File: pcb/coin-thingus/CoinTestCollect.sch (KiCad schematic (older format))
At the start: 10 parts, among them K3 AGQ200A4, K4 AGQ200A4, U3 H11AA1

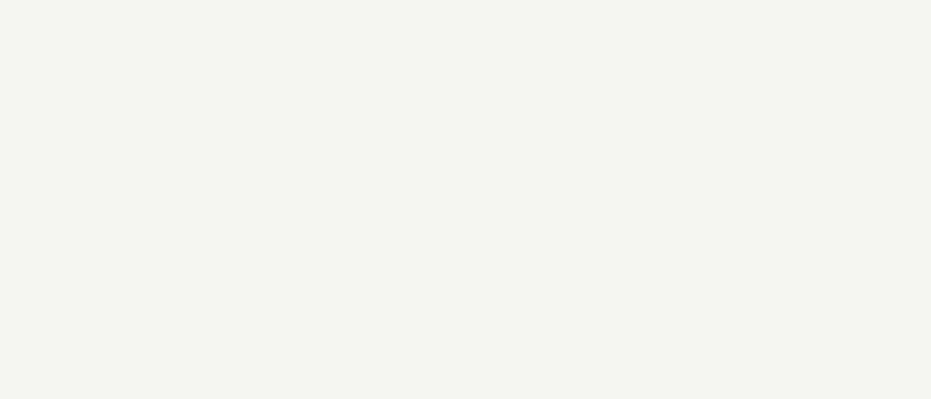
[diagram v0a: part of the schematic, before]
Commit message: Add CERN-OHL-W v2 license
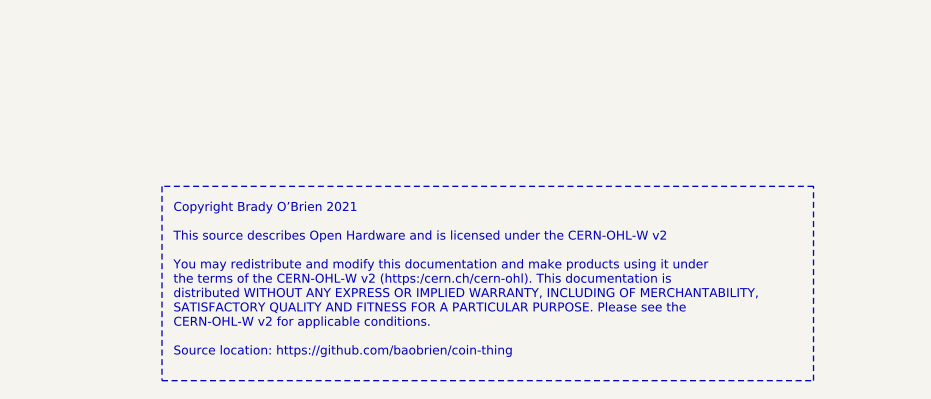
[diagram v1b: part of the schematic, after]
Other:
- note added: "Copyright Brady O’Brien 2021\n\nThis source describes Open Hardware and is licensed under the CERN-OHL-W v2\n\nYou may redistribute and modify this documentation and make products using it under\nthe terms of the CERN-OHL-W v2 (https:/cern.ch/cern-ohl). This documentation is\ndistributed WITHOUT ANY EXPRESS OR IMPLIED WARRANTY, INCLUDING OF MERCHANTABILITY,\nSATISFACTORY QUALITY AND FITNESS FOR A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"
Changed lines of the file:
@@
 Wire Wire Line
 	4050 2550 4200 2550
+Text Notes 8250 6300 0    39   ~ 0
+Copyright Brady O’Brien 2021\n\nThis source describes Open Hardware and is licensed under the CERN-OHL-W v2\n\nYou may redistribute and modify this documentation and make products using it under\nthe terms of the CERN-OHL-W v2 (https:/cern.ch/cern-ohl). This documentation is\ndistributed WITHOUT ANY EXPRESS OR IMPLIED WARRANTY, INCLUDING OF MERCHANTABILITY,\nSATISFACTORY QUALITY AND FITNESS FOR A PARTICULAR PURPOSE. Please see the\nCERN-OHL-W v2 for applicable conditions.\n\nSource location: https://github.com/baobrien/coin-thing
+Wire Notes Line
+	8200 5550 8200 6400
+Wire Notes Line
+	8200 6400 11050 6400
+Wire Notes Line
+	11050 6400 11050 5550
+Wire Notes Line
+	11050 5550 8200 5550
 $EndSCHEMATC

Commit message: Some work towards v0.2
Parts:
- removed U3: H11AA1, Package_DIP:DIP-6_W7.62mm, symbol Isolator:CNY17-1
- added U3: LTV-217, Package_SO:SOP-4_4.4x2.6mm_P1.27mm, symbol coin_trunker_parts:LTV-217
- K3: value AGQ200A4 -> HFD4/5-S
- R7: footprint Resistor_SMD:R_0612_1632Metric -> Resistor_SMD:R_1206_3216Metric
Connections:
- no-connect marks 1 -> 0
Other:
- moved on the sheet: R9
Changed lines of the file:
@@
 HV_P
-$Comp
-L Isolator:CNY17-1 U3
-U 1 1 5FA7F153
-P 8350 2900
-F 0 "U3" H 8500 3200 50  0000 C CNN
-F 1 "H11AA1" H 8350 3134 50  0000 C CNN
-F 2 "Package_DIP:DIP-6_W7.62mm" H 8350 2900 50  0001 L CNN
-F 3 "http://www.vishay.com/docs/83606/cny17.pdf" H 8350 2900 50  0001 L CNN
-	1    8350 2900
-	1    0    0    -1
-$EndComp
 $Comp
 L Device:R_US R8
@@
 F 0 "R7" H 7918 2546 50  0000 L CNN
 F 1 "3600R 2W" H 7918 2455 50  0000 L CNN
-F 2 "Resistor_SMD:R_0612_1632Metric" V 7890 2490 50  0001 C CNN
+F 2 "Resistor_SMD:R_1206_3216Metric" V 7890 2490 50  0001 C CNN
 F 3 "~" H 7850 2500 50  0001 C CNN
 	1    7850 2500
@@
 L Device:R_US R9
 U 1 1 5FAAD453
-P 8950 2700
-F 0 "R9" H 9018 2746 50  0000 L CNN
-F 1 "10K" H 9018 2655 50  0000 L CNN
-F 2 "Resistor_SMD:R_0603_1608Metric" V 8990 2690 50  0001 C CNN
-F 3 "~" H 8950 2700 50  0001 C CNN
-	1    8950 2700
+P 8950 2600
+F 0 "R9" H 9018 2646 50  0000 L CNN
+F 1 "10K" H 9018 2555 50  0000 L CNN
+F 2 "Resistor_SMD:R_0603_1608Metric" V 8990 2590 50  0001 C CNN
+F 3 "~" H 8950 2600 50  0001 C CNN
+	1    8950 2600
 	1    0    0    -1
 $EndComp
@@
 	8950 3000 8950 3100
 Wire Wire Line
-	8650 2900 8950 2900
-Wire Wire Line
-	8950 2900 8950 2850
-Wire Wire Line
-	8950 2550 8950 2350
-Wire Wire Line
-	8950 2900 9350 2900
-Connection ~ 8950 2900
-Text HLabel 9350 2900 2    50   Input ~ 0
+	8650 2800 8950 2800
+Wire Wire Line
+	8950 2800 8950 2750
+Wire Wire Line
+	8950 2450 8950 2250
+Wire Wire Line
+	8950 2800 9350 2800
+Connection ~ 8950 2800
+Text HLabel 9350 2800 2    50   Input ~ 0
 COIN_TEST
-Text HLabel 9300 2350 2    50   Input ~ 0
+Text HLabel 9300 2250 2    50   Input ~ 0
 3V3
 Wire Wire Line
-	9300 2350 8950 2350
-NoConn ~ 8650 2800
+	9300 2250 8950 2250
 Wire Wire Line
 	6800 2800 6800 4000
@@
 P 3500 2950
 F 0 "K3" V 2733 2950 50  0000 C CNN
-F 1 "AGQ200A4" V 2824 2950 50  0000 C CNN
+F 1 "HFD4/5-S" V 2824 2950 50  0000 C CNN
 F 2 "Relay_SMD:Relay_DPDT_Omron_G6K-2F-Y" H 3300 2950 50  0001 C CNN
 F 3 "" H 3300 2950 50  0001 C CNN
@@
 Wire Notes Line
 	11050 5550 8200 5550
+$Comp
+L coin_trunker_parts:LTV-217 U3
+U 1 1 6033A3B4
+P 8350 2900
+F 0 "U3" H 8350 2650 50  0000 C CNN
+F 1 "LTV-217" H 8350 3134 50  0000 C CNN
+F 2 "Package_SO:SOP-4_4.4x2.6mm_P1.27mm" H 8150 2700 50  0001 L CIN
+F 3 "http://optoelectronics.liteon.com/upload/download/DS70-2009-0014/LTV-2X7%20sereis%20Mar17.PDF" H 8350 2900 50  0001 L CNN
+	1    8350 2900
+	1    0    0    -1
+$EndComp
 $EndSCHEMATC

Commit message: HV test board; A bunch of work towards v0.2
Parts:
- D8: footprint Diode_SMD:D_SMA -> Diode_SMD:D_SOD-323_HandSoldering; Part SMAJ5938B -> BZX384-C36
- R7: footprint Resistor_SMD:R_1206_3216Metric -> Resistor_SMD:R_2010_5025Metric; Part (none) -> 2010W2J0392T4S
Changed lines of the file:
@@
 F 0 "R7" H 7918 2546 50  0000 L CNN
 F 1 "3600R 2W" H 7918 2455 50  0000 L CNN
-F 2 "Resistor_SMD:R_1206_3216Metric" V 7890 2490 50  0001 C CNN
+F 2 "Resistor_SMD:R_2010_5025Metric" V 7890 2490 50  0001 C CNN
 F 3 "~" H 7850 2500 50  0001 C CNN
+F 4 "2010W2J0392T4S" H 7850 2500 50  0001 C CNN "Part"
 	1    7850 2500
 	1    0    0    -1
@@
 F 0 "D8" H 6400 4100 50  0000 L CNN
 F 1 "36V" H 6400 3900 50  0000 L CNN
-F 2 "Diode_SMD:D_SMA" H 6450 4000 50  0001 C CNN
+F 2 "Diode_SMD:D_SOD-323_HandSoldering" H 6450 4000 50  0001 C CNN
 F 3 "~" H 6450 4000 50  0001 C CNN
-F 4 "SMAJ5938B" V 6450 4000 50  0001 C CNN "Part"
+F 4 "BZX384-C36" V 6450 4000 50  0001 C CNN "Part"
 	1    6450 4000
 	-1   0    0    1

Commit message: Bunch'o work towards v0.2
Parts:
- removed TP4: TestPoint, Connector_Pin:Pin_D1.0mm_L10.0mm, symbol Connector:TestPoint
- R7: value 3600R 2W -> 3.6K
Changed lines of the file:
@@
 P 7850 2500
 F 0 "R7" H 7918 2546 50  0000 L CNN
-F 1 "3600R 2W" H 7918 2455 50  0000 L CNN
+F 1 "3.6K" H 7918 2455 50  0000 L CNN
 F 2 "Resistor_SMD:R_2010_5025Metric" V 7890 2490 50  0001 C CNN
 F 3 "~" H 7850 2500 50  0001 C CNN
@@
 	4400 4000 4400 3600
 Connection ~ 4400 3600
-Wire Wire Line
-	2800 3350 2900 3350
 Text HLabel 9350 3000 2    50   Input ~ 0
 GND
@@
 	6450 2650 7300 2650
 $Comp
-L Connector:TestPoint TP4
-U 1 1 5FD99F71
-P 2900 3450
-F 0 "TP4" H 2842 3476 50  0000 R CNN
-F 1 "TestPoint" H 2842 3567 50  0000 R CNN
-F 2 "Connector_Pin:Pin_D1.0mm_L10.0mm" H 3100 3450 50  0001 C CNN
-F 3 "~" H 3100 3450 50  0001 C CNN
-	1    2900 3450
-	-1   0    0    1
-$EndComp
-$Comp
 L Connector:TestPoint TP3
 U 1 1 5FD9A364
@@
 Wire Wire Line
 	2900 2950 2800 2950
-Wire Wire Line
-	2900 3350 2900 3450
-Connection ~ 2900 3350
-Wire Wire Line
-	2900 3350 3200 3350
 $Comp
 L Device:D_Zener D8
@@
 	1    0    0    -1
 $EndComp
+Wire Wire Line
+	2800 3350 3200 3350
 $EndSCHEMATC

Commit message: V0.2 as ordered
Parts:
- K4: value AGQ200A4 -> HFD4/5-S
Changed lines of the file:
@@
 P 5750 2750
 F 0 "K4" V 4983 2750 50  0000 C CNN
-F 1 "AGQ200A4" V 5074 2750 50  0000 C CNN
+F 1 "HFD4/5-S" V 5074 2750 50  0000 C CNN
 F 2 "Relay_SMD:Relay_DPDT_Omron_G6K-2F-Y" H 5550 2750 50  0001 C CNN
 F 3 "" H 5550 2750 50  0001 C CNN

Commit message: Start work on alternate micro
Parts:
- R9: footprint Resistor_SMD:R_0603_1608Metric -> Resistor_SMD:R_0402_1005Metric
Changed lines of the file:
@@
 F 0 "R9" H 9018 2646 50  0000 L CNN
 F 1 "10K" H 9018 2555 50  0000 L CNN
-F 2 "Resistor_SMD:R_0603_1608Metric" V 8990 2590 50  0001 C CNN
+F 2 "Resistor_SMD:R_0402_1005Metric" V 8990 2590 50  0001 C CNN
 F 3 "~" H 8950 2600 50  0001 C CNN
 	1    8950 2600
